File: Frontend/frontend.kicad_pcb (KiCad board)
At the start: 2 copper layers, 300 parts, among them J1 PCIEx4 EDGE, J2 SWD, J3 CONN-TE-1-1337543-0, J4 UMC, J5 UMC, J6 CONN-TE-1-1337543-0, J7 UMC, J8 UMC, K1 HE3600, K10 EE2-5NU, K11 EE2-5NU, K12 EE2-5NU, K2 EE2-5NU, K3 HE3600, K4 EE2-5NU, K5 EE2-5NU, K6 EE2-5NU, K7 HE3600, K8 EE2-5NU, K9 HE3600, Q1 ULN2003AD, Q2 ULN2003AD, U1 ADA4817-1ACPZ, U10 AD8602ARZ, U11 TL972PW, U12 AD8602ARZ, U13 STM32F030C8T, U14 TL972PW, U15 AD8602ARZ, U17 MCP1700T-5002E/MB, U2 AD8003ACPZ, U24 AP3211, U26 LT1931AES5, U27 MC79M05CDT, U28 TL431AIDBZ, U29 TL431AIDBZ, U3 LMH6552SD, U4 ADA4817-1ACPZ, U5 AD8003ACPZ, U6 LMH6552SD, U8 4051-DIP, U9 TL972PW

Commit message: Route PCB
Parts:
- removed the CV1 at (-17.0, 90.5)
- removed the CV1 at (19.8, 128.3)
- removed the CV3 at (140.5, 104.5)
- removed the CV3 at (19.8, 128.3)
- removed the CV5 at (156.0, 92.0)
- removed the CV5 at (19.8, 128.3)
- removed the CV7 at (30.8, 90.5)
- removed the CV7 at (19.8, 128.3)
- removed DZ2: 43V, IPC7351-Nominal:DIOM5226X203
- removed E8: 120, IPC7351-Nominal:RESC3216X60
- removed K10, K11, K12, K8: EE2-5NU, manuf:KEMET-EE2-xNU
- removed K7, K9: HE3600, manuf:HAMLIN-HE3600
- removed L1: 6u8, manuf:BOURNS-SRN5040
- removed L2, L3: 22u, manuf:BOURNS-SRN3015
- removed Q2: ULN2003AD, IPC7351-Nominal:SOIC127P600X150-16
- removed R128: 36k, IPC7351-Nominal:RESC1608X50
- removed R129: 5k6, IPC7351-Nominal:RESC1608X50
- removed R130, R134: 10k, IPC7351-Nominal:RESC1608X50
- removed R131: 2k, IPC7351-Nominal:RESC1608X50
- removed R132, R133: 200, IPC7351-Nominal:RESC1608X50
- removed R135, R137: 120, IPC7351-Nominal:RESC1608X50
- removed R136: 30, IPC7351-Nominal:RESC1608X50
- removed U17: MCP1700T-5002E/MB, smd-semi:SOT-89
- added C100: 10n, IPC7351-Nominal:CAPC1005X55, B.Cu at (132.5, 49.0)
- added C101: 10n, IPC7351-Nominal:CAPC1005X55, B.Cu at (129.8, 43.5)
- added C102: 10n, IPC7351-Nominal:CAPC1005X55, B.Cu at (125.0, 41.5)
- added C103: 10n, IPC7351-Nominal:CAPC1005X55, B.Cu at (121.8, 36.0)
- added C104: 100n, IPC7351-Nominal:CAPC1608X55, F.Cu at (106.5, 29.2)
- added C105: 100n, IPC7351-Nominal:CAPC1220X107, B.Cu at (124.5, 26.5)
- added C106: 10n, IPC7351-Nominal:CAPC1005X55, B.Cu at (121.0, 46.0)
- added C107: 10n, IPC7351-Nominal:CAPC1005X55, B.Cu at (126.2, 48.5)
- added C108: 10n, IPC7351-Nominal:CAPC1005X55, B.Cu at (130.1, 49.0)
- added C109: 10n, IPC7351-Nominal:CAPC1005X55, B.Cu at (132.0, 43.5)
- added C110: 10n, IPC7351-Nominal:CAPC1005X55, B.Cu at (122.5, 41.5)
- added C111: 10n, IPC7351-Nominal:CAPC1005X55, B.Cu at (124.2, 36.0)
- added C112: 100n, IPC7351-Nominal:CAPC1608X55, F.Cu at (116.8, 26.2)
- added C113: 100n, IPC7351-Nominal:CAPC1608X55, F.Cu at (126.8, 67.5)
- added C89: 100n, IPC7351-Nominal:CAPC1220X107, F.Cu at (131.5, 31.5)
- added C90: 100n, IPC7351-Nominal:CAPC1220X107, F.Cu at (133.8, 40.8)
- added C91: 100n, IPC7351-Nominal:CAPC1220X107, F.Cu at (134.5, 38.0)
- added C92: 33u/16, IPC7351-Nominal:CAPMP7343X310, F.Cu at (140.8, 39.2)
- added C93: 100n, IPC7351-Nominal:CAPC1220X107, F.Cu at (124.8, 55.5)
- added C94: 100n, IPC7351-Nominal:CAPC1220X107, F.Cu at (134.2, 33.8)
- added C95: 100n, IPC7351-Nominal:CAPC1220X107, F.Cu at (128.0, 40.5)
- added C96: 100n, IPC7351-Nominal:CAPC1220X107, F.Cu at (125.8, 33.2)
- added C97: 100n, IPC7351-Nominal:CAPC1220X107, B.Cu at (127.5, 26.5)
- added C98: 10n, IPC7351-Nominal:CAPC1005X55, B.Cu at (121.0, 48.5)
- added C99: 10n, IPC7351-Nominal:CAPC1005X55, B.Cu at (126.2, 45.2)
- added CV1: 30p, CV8, F.Cu at (114.5, 95.0)
- added CV3: 30p, CV8, F.Cu at (83.5, 72.0)
- added CV5: 30p, CV8, F.Cu at (114.5, 49.0)
- added CV7: 30p, CV8, F.Cu at (83.5, 26.0)
- added D6: BAV99W, smd-semi:SC-70, F.Cu at (113.0, 22.5)
- added D7: BAV99W, smd-semi:SC-70, F.Cu at (116.5, 23.5)
- added J10: SWD, conn-100mil:CONN-100MIL-M-2x5-SHROUD, F.Cu at (150.8, 57.5)
- added J11: APWR, conn-100mil:CONN-100MIL-M-1x4-SHROUD, B.Cu at (159.0, 25.8)
- added J9: PCIEx4 EDGE, w_conn_pc:pci-x_edge-x4, F.Cu at (110.0, 114.0)
- added U19: LM317S, smd-semi:TO-263, F.Cu at (151.0, 85.7)
- added U20: L78M05CDT, smd-semi:TO-252, F.Cu at (137.0, 26.0)
- added U21: MCP1700T-3302E/TT, smd-semi:SOT-23, F.Cu at (136.2, 72.0)
- added U22: MC79M05CDT, smd-semi:TO-252, F.Cu at (157.3, 39.6)
- added U23: MCP9700T-E/TT, smd-semi:SOT-23, F.Cu at (68.5, 55.5)
- added U25: MAX4567EEE, IPC7351-Nominal:SOP63P600X160-16, F.Cu at (123.8, 47.0)
- added U7: LMH6552SD, IPC7351-Nominal:PSON50P300X250X80-9, F.Cu at (126.0, 73.8)
- C1: value 6p8 -> 1u; footprint IPC7351-Nominal:CAPC1608X55 -> IPC7351-Nominal:CAPC2012X70
- C11: value 100n -> 33u/16; footprint IPC7351-Nominal:CAPC1608X55 -> IPC7351-Nominal:CAPMP7343X310
- C12, C13, C14, C15: footprint IPC7351-Nominal:CAPC1608X55 -> IPC7351-Nominal:CAPC1220X107
- C16: value 10p 1kV -> 33u/16; footprint IPC7351-Nominal:CAPC3216X70 -> IPC7351-Nominal:CAPMP7343X310
- C17: value 22n 630V -> 100n; footprint manuf:MANUF-PANASONIC-ECQ-EF -> IPC7351-Nominal:CAPC1220X107
- C18: value 6p8 -> 100n; footprint IPC7351-Nominal:CAPC1608X55 -> IPC7351-Nominal:CAPC1220X107; moved to F.Cu
- C19: value 4p7 1kV -> 100n; footprint IPC7351-Nominal:CAPC3216X70 -> IPC7351-Nominal:CAPC1220X107
- C2: value 22n 630V -> 6p8; footprint manuf:MANUF-PANASONIC-ECQ-EF -> IPC7351-Nominal:CAPC1608X55
- C20: value 10p 1kV -> 100n; footprint IPC7351-Nominal:CAPC3216X70 -> IPC7351-Nominal:CAPC1220X107
- C21: value 120p -> 100n; footprint IPC7351-Nominal:CAPC2012X70 -> IPC7351-Nominal:CAPC1220X107; moved to B.Cu
- C22, C23, C24, C25, C26, C27, C30, C31, C32, C33, C34: value 100n -> 10n; footprint IPC7351-Nominal:CAPC1608X55 -> IPC7351-Nominal:CAPC1005X55; moved to B.Cu
- C29: footprint IPC7351-Nominal:CAPC1608X55 -> IPC7351-Nominal:CAPC1220X107; moved to B.Cu
- C35: value 100n -> 10n; footprint pth-passive:C-FILM-2.5mm -> IPC7351-Nominal:CAPC1005X55; moved to B.Cu
- C37, C43: value 100n -> 15u/16; footprint pth-passive:C-FILM-2.5mm -> IPC7351-Nominal:CAPMP3528X210
- C38: value 100n -> 1u; footprint pth-passive:C-FILM-2.5mm -> IPC7351-Nominal:CAPC2012X70; moved to B.Cu
- C39: footprint pth-passive:C-FILM-2.5mm -> IPC7351-Nominal:CAPC1608X55
- C4: value 4p7 1kV -> 22n 630V; footprint IPC7351-Nominal:CAPC3216X70 -> manuf:MANUF-PANASONIC-ECQ-EF; moved to F.Cu
- C40, C42, C47, E5, J7, J8: moved to B.Cu
- C41: footprint pth-passive:C-FILM-2.5mm -> IPC7351-Nominal:CAPC1608X55; moved to B.Cu
- C44: value 10n -> 100n; footprint IPC7351-Nominal:CAPC2012X70 -> IPC7351-Nominal:CAPC1608X55
- C45: value 220u -> 15u/16; footprint pth-passive:C-ALUM-8mm -> IPC7351-Nominal:CAPMP3528X210
- C46: value 10u -> 1u; footprint IPC7351-Nominal:CAPC3216X70 -> IPC7351-Nominal:CAPC2012X70
- C48: value 47u -> 10n; footprint pth-passive:C-ALUM-5mm -> IPC7351-Nominal:CAPC1005X55
- C49: value 100n -> 10n; footprint IPC7351-Nominal:CAPC1608X55 -> IPC7351-Nominal:CAPC1005X55
- C5, R1: moved to F.Cu
- C50: value 22u -> 100n; footprint IPC7351-Nominal:CAPC3216X70 -> IPC7351-Nominal:CAPC1608X55
- C52, C54, C62, C64, C68: value 47u -> 100n; footprint pth-passive:C-ALUM-5mm -> IPC7351-Nominal:CAPC1608X55
- C55: value 1u -> 15u/16; footprint IPC7351-Nominal:CAPC3216X70 -> IPC7351-Nominal:CAPMP3528X210
- C56: value 220u -> 100n; footprint pth-passive:C-ALUM-8mm -> IPC7351-Nominal:CAPC1608X55
- C57: value 10u -> 100n; footprint IPC7351-Nominal:CAPC3216X70 -> IPC7351-Nominal:CAPC1608X55
- C6: value 120p -> 4p7 1kV; footprint IPC7351-Nominal:CAPC2012X70 -> IPC7351-Nominal:CAPC3216X70
- C60: value 22u -> 15u/16; footprint IPC7351-Nominal:CAPC3216X70 -> IPC7351-Nominal:CAPMP3528X210
- C66: value 470p -> 47u; footprint IPC7351-Nominal:CAPC1608X55 -> pth-passive:C-ALUM-5mm
- C69: value 4p7 1kV -> 47u; footprint IPC7351-Nominal:CAPC3216X70 -> pth-passive:C-ALUM-5mm
- C7: value 100n -> 10p 1kV; footprint IPC7351-Nominal:CAPC1608X55 -> IPC7351-Nominal:CAPC3216X70
- C70: value 10p 1kV -> 47u; footprint IPC7351-Nominal:CAPC3216X70 -> pth-passive:C-ALUM-5mm; moved to F.Cu
- C71, C72: value 22u -> 1u; footprint IPC7351-Nominal:CAPC3216X70 -> IPC7351-Nominal:CAPC2012X70
- C73, C75, C76: value 100n -> 47u; footprint IPC7351-Nominal:CAPC1608X55 -> pth-passive:C-ALUM-5mm
- C78: value 1u -> 6p8; footprint IPC7351-Nominal:CAPC2012X70 -> IPC7351-Nominal:CAPC1608X55
- C79: value 1u -> 4p7 1kV; footprint IPC7351-Nominal:CAPC2012X70 -> IPC7351-Nominal:CAPC3216X70
- C8: value 100n -> 120p; footprint IPC7351-Nominal:CAPC1608X55 -> IPC7351-Nominal:CAPC2012X70; moved to B.Cu
- C80: value 1u -> 22n 630V; footprint IPC7351-Nominal:CAPC2012X70 -> manuf:MANUF-PANASONIC-ECQ-EF
- C81, C83: value 1u -> 10p 1kV; footprint IPC7351-Nominal:CAPC2012X70 -> IPC7351-Nominal:CAPC3216X70
- C82: value 1u -> 4p7 1kV; footprint IPC7351-Nominal:CAPC2012X70 -> IPC7351-Nominal:CAPC3216X70; moved to B.Cu
- C84: value 1u -> 120p; moved to B.Cu
- C85, C86: value 1u -> 100n; footprint IPC7351-Nominal:CAPC2012X70 -> IPC7351-Nominal:CAPC1608X55
- C87: value 1u -> 33u/16; footprint IPC7351-Nominal:CAPC2012X70 -> IPC7351-Nominal:CAPMP7343X310
- C88: value 1u -> 100n; footprint IPC7351-Nominal:CAPC2012X70 -> IPC7351-Nominal:CAPC1220X107
- CV2, CV4, CV6, CV8: footprint CV1 -> CV8
- D1, D2: value BAV99 -> BAV99W; footprint smd-semi:SOT-23 -> smd-semi:SC-70
- D3: value S1A -> BAV99W; footprint IPC7351-Nominal:DIOM5326X292 -> smd-semi:SC-70
- D4: value MBR0520 -> US1A; footprint smd-semi:SOD-123 -> IPC7351-Nominal:DIOM5326X292
- D5: value MBR0520 -> BAV99W; footprint smd-semi:SOD-123 -> smd-semi:SC-70
- E2, E3: value 120 -> BEAD-0603; footprint IPC7351-Nominal:RESC3216X60 -> IPC7351-Nominal:INDC1608X95
- J1: value PCIEx4 EDGE -> VOCM; footprint conn-fci:CONN-10018784-10201TLF-PCIEx4-FCI -> conn-100mil:CONN-100MIL-M-1x2; moved to B.Cu
- J2: value SWD -> BNC; footprint conn-100mil:CONN-100MIL-M-2x5-SHROUD -> manuf:CONN-BNC-1-1337543-0
- J3: value CONN-TE-1-1337543-0 -> UMC; footprint manuf:CONN-BNC-1-1337543-0 -> conn-molex:CONN-MOLEX-0734120110; moved to B.Cu
- J5: value UMC -> VOCM; footprint conn-molex:CONN-MOLEX-0734120110 -> conn-100mil:CONN-100MIL-M-1x2
- J6: value CONN-TE-1-1337543-0 -> BNC
- K4, K6: value EE2-5NU -> HE3600; footprint manuf:KEMET-EE2-xNU -> manuf:HAMLIN-HE3600
- MP1: value SHIELD -> 217-36CTE6; footprint manuf:LAIRD-BMI-S-203 -> MP1
- R10: value 523k -> 536k
- R100: value 430 -> 200; footprint IPC7351-Nominal:RESC1608X50 -> IPC7351-Nominal:RESC3216X60
- R101: value 1k -> 200; footprint IPC7351-Nominal:RESC1608X50 -> IPC7351-Nominal:RESC3216X60
- R102, R103: value 10k -> 200; footprint IPC7351-Nominal:RESC1608X50 -> IPC7351-Nominal:RESC3216X60
- R104: value 20k -> 10M; moved to B.Cu
- R105: value 430 -> 3k3; footprint IPC7351-Nominal:RESC1608X50 -> IPC7351-Nominal:RESC1005X40
- R106, R107: value 1k -> 357k; footprint IPC7351-Nominal:RESC1608X50 -> IPC7351-Nominal:RESC2012X50; moved to B.Cu
- R108: value 10k -> 150; footprint IPC7351-Nominal:RESC1608X50 -> IPC7351-Nominal:RESC1005X40
- R109: value 20k -> 348k; footprint IPC7351-Nominal:RESC1608X50 -> IPC7351-Nominal:RESC2012X50; moved to B.Cu
- R11: value 536k -> 100k; footprint IPC7351-Nominal:RESC2012X50 -> IPC7351-Nominal:RESC1608X50; moved to F.Cu
- R110: value 30k -> 10M; moved to B.Cu
- R111: value 1k -> 348k; footprint IPC7351-Nominal:RESC1608X50 -> IPC7351-Nominal:RESC2012X50; moved to B.Cu
- R112: value 3k3 -> 150; footprint IPC7351-Nominal:RESC1608X50 -> IPC7351-Nominal:RESC1005X40
- R113: value 3k3 -> 443; footprint IPC7351-Nominal:RESC1608X50 -> IPC7351-Nominal:RESC1005X40
- R114, R124: value 10k -> 49R9; footprint IPC7351-Nominal:RESC1608X50 -> IPC7351-Nominal:RESC1005X40
- R115: value 10k -> 165; footprint IPC7351-Nominal:RESC1608X50 -> IPC7351-Nominal:RESC1005X40
- R116: value 20k -> 443; footprint IPC7351-Nominal:RESC1608X50 -> IPC7351-Nominal:RESC1005X40
- R117: value 30k -> 64R9; footprint IPC7351-Nominal:RESC1608X50 -> IPC7351-Nominal:RESC1005X40
- R118: value 10k -> 300; footprint IPC7351-Nominal:RESC1608X50 -> IPC7351-Nominal:RESC1005X40
- R119: value 10k -> 35R7; footprint IPC7351-Nominal:RESC1608X50 -> IPC7351-Nominal:RESC1005X40
- R12: value 357k -> 10M; footprint IPC7351-Nominal:RESC2012X50 -> IPC7351-Nominal:RESC1608X50; moved to F.Cu
- R120: value 10k -> 64R9; footprint IPC7351-Nominal:RESC1608X50 -> IPC7351-Nominal:RESC1005X40
- R121: value 20k -> 300; footprint IPC7351-Nominal:RESC1608X50 -> IPC7351-Nominal:RESC1005X40
- R122: value 100 -> 150; footprint IPC7351-Nominal:RESC1608X50 -> IPC7351-Nominal:RESC1005X40
- R123: value 10k -> 443; footprint IPC7351-Nominal:RESC1608X50 -> IPC7351-Nominal:RESC1005X40
- R125: value 20k -> 120k; footprint IPC7351-Nominal:RESC1608X50 -> IPC7351-Nominal:RESC1005X40
- R126: value 100 -> 443; footprint IPC7351-Nominal:RESC1608X50 -> IPC7351-Nominal:RESC1005X40
- R127: value 120 -> 30k; footprint IPC7351-Nominal:RESC1608X50 -> IPC7351-Nominal:RESC1005X40
- R14: value 200 -> 357k; footprint IPC7351-Nominal:RESC3216X60 -> IPC7351-Nominal:RESC2012X50; moved to B.Cu
- R18: value 100k -> 200; footprint IPC7351-Nominal:RESC1608X50 -> IPC7351-Nominal:RESC3216X60
- R19: value 357k -> 10M; footprint IPC7351-Nominal:RESC2012X50 -> IPC7351-Nominal:RESC1608X50
- R20: value 357k -> 3k3; footprint IPC7351-Nominal:RESC2012X50 -> IPC7351-Nominal:RESC1005X40; moved to F.Cu
- R21: value 348k -> 357k
- R22: value 10M -> 357k
- R23: value 348k -> 150; footprint IPC7351-Nominal:RESC2012X50 -> IPC7351-Nominal:RESC1005X40; moved to F.Cu
- R24: value 10M -> 348k; moved to B.Cu
- R25: value 120 -> 10M; moved to B.Cu
- R26: value 120 -> 348k; footprint IPC7351-Nominal:RESC1608X50 -> IPC7351-Nominal:RESC2012X50; moved to B.Cu
- R27: value 443 -> 150; footprint IPC7351-Nominal:RESC1608X50 -> IPC7351-Nominal:RESC1005X40
- R28: value 49r9 -> 443; footprint IPC7351-Nominal:RESC1608X50 -> IPC7351-Nominal:RESC1005X40
- R29: value 30 -> 49R9; footprint IPC7351-Nominal:RESC1608X50 -> IPC7351-Nominal:RESC1005X40
- R30, R33, R35, R38, R4: footprint IPC7351-Nominal:RESC1608X50 -> IPC7351-Nominal:RESC1005X40
- R31: value 30 -> 443; footprint IPC7351-Nominal:RESC1608X50 -> IPC7351-Nominal:RESC1005X40
- R32: value 30 -> 64R9; footprint IPC7351-Nominal:RESC1608X50 -> IPC7351-Nominal:RESC1005X40
- R34: value 300 -> 35R7; footprint IPC7351-Nominal:RESC1608X50 -> IPC7351-Nominal:RESC1005X40
- R36: value 64R9 -> 300; footprint IPC7351-Nominal:RESC1608X50 -> IPC7351-Nominal:RESC1005X40
- R37: value 120 -> 150; footprint IPC7351-Nominal:RESC1608X50 -> IPC7351-Nominal:RESC1005X40
- R39: value 49r9 -> 49R9; footprint IPC7351-Nominal:RESC1608X50 -> IPC7351-Nominal:RESC1005X40
- R40: value 200 -> 120k; footprint IPC7351-Nominal:RESC1608X50 -> IPC7351-Nominal:RESC1005X40
- R41: value 35R7 -> 443; footprint IPC7351-Nominal:RESC1608X50 -> IPC7351-Nominal:RESC1005X40
- R42: value 432 -> 30k; footprint IPC7351-Nominal:RESC1608X50 -> IPC7351-Nominal:RESC1005X40
- R43, R44: value 75 -> 10k
- R45: value 1M -> 10k
- R46: value 120 -> 47k
- R47, R48: value 332k -> 47k; footprint IPC7351-Nominal:RESC2012X50 -> IPC7351-Nominal:RESC1608X50
- R49: value 332k -> 10k; footprint IPC7351-Nominal:RESC2012X50 -> IPC7351-Nominal:RESC1005X40
- R50: value 3k3 -> 33k; footprint IPC7351-Nominal:RESC1608X50 -> IPC7351-Nominal:RESC1005X40
- R51: value 523k -> 10k; footprint IPC7351-Nominal:RESC2012X50 -> IPC7351-Nominal:RESC1005X40
- R52: value 523k -> 33k; footprint IPC7351-Nominal:RESC2012X50 -> IPC7351-Nominal:RESC1005X40
- R53: value 536k -> 20k; footprint IPC7351-Nominal:RESC2012X50 -> IPC7351-Nominal:RESC1005X40
- R54: value 357k -> 5k6; footprint IPC7351-Nominal:RESC2012X50 -> IPC7351-Nominal:RESC1005X40
- R55: value 357k -> 20k; footprint IPC7351-Nominal:RESC2012X50 -> IPC7351-Nominal:RESC1005X40
- R56, R57, R58, R59: value 200 -> 5k6; footprint IPC7351-Nominal:RESC3216X60 -> IPC7351-Nominal:RESC1005X40
- R60: value 100k -> 5k6; footprint IPC7351-Nominal:RESC1608X50 -> IPC7351-Nominal:RESC1005X40
- R61: value 357k -> 10k; footprint IPC7351-Nominal:RESC2012X50 -> IPC7351-Nominal:RESC1005X40
- R62: value 357k -> 680; footprint IPC7351-Nominal:RESC2012X50 -> IPC7351-Nominal:RESC1005X40
- R63: value 348k -> 10k; footprint IPC7351-Nominal:RESC2012X50 -> IPC7351-Nominal:RESC1005X40
- R64: value 10M -> 680; footprint IPC7351-Nominal:RESC2012X50 -> IPC7351-Nominal:RESC1005X40
- R65: value 348k -> 20k; footprint IPC7351-Nominal:RESC2012X50 -> IPC7351-Nominal:RESC1005X40
- R66, R82: value 30 -> 5k6; footprint IPC7351-Nominal:RESC1608X50 -> IPC7351-Nominal:RESC1005X40
- R67: value 33 -> 20k; footprint IPC7351-Nominal:RESC1608X50 -> IPC7351-Nominal:RESC1005X40
- R68, R72: value 120 -> 5k6; footprint IPC7351-Nominal:RESC1608X50 -> IPC7351-Nominal:RESC1005X40
- R69, R80: value 443 -> 5k6; footprint IPC7351-Nominal:RESC1608X50 -> IPC7351-Nominal:RESC1005X40
- R70, R81: value 49r9 -> 5k6; footprint IPC7351-Nominal:RESC1608X50 -> IPC7351-Nominal:RESC1005X40
- R71: value 10M -> 5k6; footprint IPC7351-Nominal:RESC2012X50 -> IPC7351-Nominal:RESC1005X40; moved to F.Cu
- R73: value 30 -> 10k; footprint IPC7351-Nominal:RESC1608X50 -> IPC7351-Nominal:RESC1005X40; moved to F.Cu
- R74: value 165 -> 100; footprint IPC7351-Nominal:RESC1608X50 -> IPC7351-Nominal:RESC1005X40; moved to F.Cu
- R75: value 300 -> 10k; footprint IPC7351-Nominal:RESC1608X50 -> IPC7351-Nominal:RESC1005X40
- R76: value 300 -> 100; footprint IPC7351-Nominal:RESC1608X50 -> IPC7351-Nominal:RESC1005X40
- R77: value 64R9 -> 20k; footprint IPC7351-Nominal:RESC1608X50 -> IPC7351-Nominal:RESC1005X40
- R78: value 64R9 -> 5k6; footprint IPC7351-Nominal:RESC1608X50 -> IPC7351-Nominal:RESC1005X40
- R79: value 120 -> 20k; footprint IPC7351-Nominal:RESC1608X50 -> IPC7351-Nominal:RESC1005X40
- R8: value 3k3 -> 523k; footprint IPC7351-Nominal:RESC1608X50 -> IPC7351-Nominal:RESC2012X50; moved to B.Cu
- R83: value 30 -> 15 2W; footprint IPC7351-Nominal:RESC1608X50 -> manuf:KOASPEER-MOS-2W
- R84: value 432 -> 120
- R85: value 200 -> 430; moved to F.Cu
- R86: value 15k -> 75
- R87: value 10k -> 75
- R88: value 35R7 -> 1M; moved to F.Cu
- R89: value 15k -> 33; footprint IPC7351-Nominal:RESC1608X50 -> IPC7351-Nominal:RESC1005X40
- R90, R91: value 10k -> 332k; footprint IPC7351-Nominal:RESC1608X50 -> IPC7351-Nominal:RESC2012X50
- R92: value 120 -> 332k; footprint IPC7351-Nominal:RESC1608X50 -> IPC7351-Nominal:RESC2012X50
- R93, R94: value 47k -> 523k; footprint IPC7351-Nominal:RESC1608X50 -> IPC7351-Nominal:RESC2012X50; moved to B.Cu
- R95: value 47k -> 536k; footprint IPC7351-Nominal:RESC1608X50 -> IPC7351-Nominal:RESC2012X50; moved to B.Cu
- R96: value 10k -> 100k
- R97: value 10k -> 10M
- R98: value 10k -> 357k; footprint IPC7351-Nominal:RESC1608X50 -> IPC7351-Nominal:RESC2012X50; moved to B.Cu
- R99: value 20k -> 357k; footprint IPC7351-Nominal:RESC1608X50 -> IPC7351-Nominal:RESC2012X50; moved to B.Cu
- U1: value ADA4817-1ACPZ -> MCP9700T-E/TT; footprint manuf:ANALOG-LFCSP_VD-8 -> smd-semi:SOT-23
- U10: value AD8602ARZ -> STM32F030C8T; footprint IPC7351-Nominal:SOIC127P600X175-8 -> IPC7351-Nominal:QFP50P900X900X160-48
- U11, U14: value TL972PW -> MC33078DGK; footprint IPC7351-Nominal:SOP65P640X120-8 -> IPC7351-Nominal:SOP65P490X109-8
- U12, U15: value AD8602ARZ -> MC33078DGK; footprint IPC7351-Nominal:SOIC127P600X175-8 -> IPC7351-Nominal:SOP65P490X109-8
- U13: value STM32F030C8T -> MC33078DGK; footprint IPC7351-Nominal:QFP50P900X900X160-48 -> IPC7351-Nominal:SOP65P490X109-8
- U2: value AD8003ACPZ -> ADA4817-1ACPZ; footprint IPC7351-Nominal:QFN50P400X400X80-25 -> manuf:ANALOG-LFCSP_VD-8
- U24: value AP3211 -> ADA4817-1ACPZ; footprint smd-semi:SOT-23-6 -> manuf:ANALOG-LFCSP_VD-8
- U26: value LT1931AES5 -> MAX4567EEE; footprint smd-semi:SOT-23-5 -> IPC7351-Nominal:SOP63P600X160-16
- U27: value MC79M05CDT -> AD8003ACPZ; footprint smd-semi:TO-252 -> IPC7351-Nominal:QFN50P400X400X80-25
- U28: value TL431AIDBZ -> MAX4567EEE; footprint smd-semi:SOT-23 -> IPC7351-Nominal:SOP63P600X160-16
- U29: value TL431AIDBZ -> LMH6552SD; footprint smd-semi:SOT-23 -> IPC7351-Nominal:PSON50P300X250X80-9
- U3, U6: value LMH6552SD -> MAX4567EEE; footprint IPC7351-Nominal:PSON50P300X250X80-9 -> IPC7351-Nominal:SOP63P600X160-16
- U4: value ADA4817-1ACPZ -> MAX4567EEE; footprint manuf:ANALOG-LFCSP_VD-8 -> IPC7351-Nominal:SOP63P600X160-16
- U8: value 4051-DIP -> MC33078DGK; footprint dip-sip:DIP-16 -> IPC7351-Nominal:SOP65P490X109-8
- U9: value TL972PW -> MAX5725AAUP; footprint IPC7351-Nominal:SOP65P640X120-8 -> IPC7351-Nominal:SOP65P640X110-20
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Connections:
- C1 pad 1: Net-(C1-Pad1) -> +5
- C1 pad 2: Net-(C1-Pad2) -> GND
- C10 pad 1: +5 -> Net-(C10-Pad1)
- C12 pad 1: -5 -> +5
- C13 pad 1: -5 -> +5
- C14 pad 1: -5 -> +5
- C15 pad 1: -5 -> +5
- C16 pad 1: Net-(C16-Pad1) -> GND
- C16 pad 2: Net-(C16-Pad2) -> -5
- C17 pad 1: Net-(C17-Pad1) -> GND
- C17 pad 2: Net-(C17-Pad2) -> -5
- C18 pad 1: Net-(C18-Pad1) -> GND
- C18 pad 2: Net-(C18-Pad2) -> -5
- C19 pad 1: Net-(C19-Pad1) -> GND
- C19 pad 2: Net-(C19-Pad2) -> -5
- C20 pad 1: Net-(C19-Pad2) -> GND
- C20 pad 2: Net-(C20-Pad2) -> -5
- C21 pad 1: Net-(C19-Pad1) -> +5
- C22 pad 1: Net-(C22-Pad1) -> +5
- C27 pad 1: -5 -> +5
- C28 pad 1: -5 -> +8
- C29 pad 1: -5 -> GND
- C29 pad 2: GND -> -5
- C3 pad 2: Net-(C16-Pad1) -> Net-(C3-Pad2)
- C30 pad 1: -5 -> GND
- C30 pad 2: GND -> -5
- C31 pad 1: Net-(C31-Pad1) -> GND
- C31 pad 2: GND -> -5
- C32 pad 1: Net-(C32-Pad1) -> GND
- C32 pad 2: GND -> -5
- C33 pad 1: +2.5 -> GND
- C33 pad 2: GND -> -5
- C34 pad 1: Net-(C34-Pad1) -> GND
- C34 pad 2: GND -> -5
- C35 pad 1: Net-(C35-Pad1) -> GND
- C35 pad 2: GND -> -5
- C36 pad 1: Net-(C36-Pad1) -> GND
- C36 pad 2: GND -> -8
- C37 pad 1: Net-(C37-Pad1) -> +3.3
- C38 pad 1: Net-(C38-Pad1) -> +3.3
- C39 pad 1: Net-(C39-Pad1) -> +3.3
- C40 pad 1: Net-(C40-Pad1) -> +3.3
- C41 pad 1: Net-(C41-Pad1) -> +3.3
- C42 pad 1: Net-(C42-Pad1) -> +3.3
- C43 pad 1: Net-(C43-Pad1) -> /Microcontroller/3V3DAC
- C44 pad 1: Net-(C44-Pad1) -> GND
- C44 pad 2: Net-(C44-Pad2) -> /Microcontroller/3V3DAC
- C45 pad 1: Net-(C45-Pad1) -> /Microcontroller/3V3ADC
- C46 pad 1: Net-(C45-Pad1) -> /Microcontroller/3V3ADC
- C47 pad 1: Net-(C45-Pad1) -> GND
- C47 pad 2: GND -> /Microcontroller/3V3ADC
- C48 pad 1: Net-(C48-Pad1) -> /Channel1/VOS1
- C48 pad 2: GND -> Net-(C48-Pad2)
- C49 pad 1: Net-(C49-Pad1) -> /Channel2/VOS1
- C49 pad 2: GND -> Net-(C49-Pad2)
- C5 pad 1: Net-(C4-Pad2) -> Net-(C3-Pad2)
- C50 pad 1: Net-(C49-Pad1) -> -2.5
- C50 pad 2: GND -> Net-(C50-Pad2)
- C51 pad 1: Net-(C51-Pad1) -> /Channel1/VOS2
- C51 pad 2: GND -> Net-(C51-Pad2)
- C52 pad 1: Net-(C51-Pad1) -> /Channel2/VOS2
- C52 pad 2: GND -> Net-(C52-Pad2)
- C53 pad 1: Net-(C53-Pad1) -> /Channel1/VOS3
- C53 pad 2: GND -> Net-(C53-Pad2)
- C54 pad 1: Net-(C53-Pad1) -> /Channel2/VOS3
- C54 pad 2: GND -> Net-(C54-Pad2)
- C55 pad 1: Net-(C55-Pad1) -> +8
- C55 pad 2: Net-(C55-Pad2) -> GND
- C56 pad 1: Net-(C56-Pad1) -> +8
- C57 pad 1: Net-(C56-Pad1) -> +8
- C58 pad 1: Net-(C56-Pad1) -> +8
- C59 pad 1: Net-(C59-Pad1) -> +8
- C6 pad 1: Net-(C4-Pad1) -> Net-(C6-Pad1)
- C6 pad 2: GND -> Net-(C6-Pad2)
- C60 pad 1: Net-(C59-Pad1) -> GND
- C60 pad 2: GND -> -8
- C61 pad 1: Net-(C61-Pad1) -> GND
- C61 pad 2: GND -> -8
- C62 pad 2: Net-(C61-Pad1) -> -8
- C63 pad 1: Net-(C63-Pad1) -> GND
- C63 pad 2: GND -> -8
- C64 pad 2: Net-(C63-Pad1) -> -8
- C65 pad 1: GND -> Net-(C65-Pad1)
- C65 pad 2: -5 -> GND
- C66 pad 1: Net-(C59-Pad1) -> /Power/VRHS
- C66 pad 2: Net-(C66-Pad2) -> GND
- C67 pad 1: +2.5 -> +8
- C68 pad 1: GND -> Net-(C68-Pad1)
- C68 pad 2: -2.5 -> GND
- C69 pad 1: Net-(C69-Pad1) -> Net-(C68-Pad1)
- C69 pad 2: Net-(C69-Pad2) -> GND
- C7 pad 1: Net-(C7-Pad1) -> Net-(C6-Pad2)
- C7 pad 2: GND -> Net-(C7-Pad2)
- C70 pad 1: Net-(C69-Pad2) -> +5
- C70 pad 2: Net-(C70-Pad2) -> GND
- C72 pad 1: +3.3 -> +3.3A
- C73 pad 1: +3.3 -> GND
- C73 pad 2: GND -> -8
- C74 pad 1: +3.3 -> Net-(C74-Pad1)
- C75 pad 1: +3.3 -> GND
- C75 pad 2: GND -> Net-(C74-Pad1)
- C76 pad 1: +3.3 -> GND
- C76 pad 2: GND -> -5
- C78 pad 1: +5 -> Net-(C78-Pad1)
- C78 pad 2: GND -> Net-(C78-Pad2)
- C79 pad 1: +5 -> Net-(C79-Pad1)
- C79 pad 2: GND -> Net-(C79-Pad2)
- C8 pad 1: +5 -> Net-(C6-Pad1)
- C80 pad 1: +5 -> Net-(C80-Pad1)
- C80 pad 2: GND -> Net-(C80-Pad2)
- C81 pad 1: +5 -> Net-(C79-Pad2)
- C81 pad 2: GND -> Net-(C81-Pad2)
- C82 pad 1: +5 -> Net-(C82-Pad1)
- C82 pad 2: GND -> Net-(C82-Pad2)
- C83 pad 1: GND -> Net-(C82-Pad2)
- C83 pad 2: -5 -> Net-(C83-Pad2)
- C84 pad 1: GND -> Net-(C82-Pad1)
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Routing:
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- added copper zone on F.Cu, net +5
- added copper zone on F.Cu, net -5
- added copper zone on F.Cu, net /Power/VRHS
- added copper zone on F.Cu, net GND
- added copper zone on In1.Cu, net GND
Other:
- board outline added: 100 x 100.2 mm
- copper layers 2 -> 4
- net class Default: clearance 0.2 -> 0.18
- rule trace_clearance: 0.2 -> 0.18

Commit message: Work more on routing
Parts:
- added DS1: LED-0603, smd-semi:LED-0603, F.Cu at (64.5, 61.0)
- added DS10: LED-0603, smd-semi:LED-0603, F.Cu at (128.5, 104.0)
- added DS11: LED-0603, smd-semi:LED-0603, F.Cu at (128.5, 107.0)
- added DS12: LED-0603, smd-semi:LED-0603, F.Cu at (128.5, 105.5)
- added DS2: LED-0603, smd-semi:LED-0603, F.Cu at (64.5, 62.5)
- added DS3: LED-0603, smd-semi:LED-0603, F.Cu at (64.5, 64.0)
- added DS4: LED-0603, smd-semi:LED-0603, F.Cu at (64.5, 65.5)
- added DS5: LED-0603, smd-semi:LED-0603, F.Cu at (64.5, 67.0)
- added DS6: LED-0603, smd-semi:LED-0603, F.Cu at (64.5, 68.5)
- added DS7: LED-0603, smd-semi:LED-0603, F.Cu at (143.2, 48.0)
- added DS8: LED-0603, smd-semi:LED-0603, F.Cu at (143.2, 46.5)
- added DS9: LED-0603, smd-semi:LED-0603, F.Cu at (143.2, 49.5)
- added G***: LOGO, LOGO, F.Cu at (68.0, 25.0)
- added R128: 3k3, IPC7351-Nominal:RESC1005X40, F.Cu at (68.0, 61.0)
- added R129: 3k3, IPC7351-Nominal:RESC1005X40, F.Cu at (68.0, 62.5)
- added R130: 3k3, IPC7351-Nominal:RESC1005X40, F.Cu at (68.0, 64.0)
- added R131: 3k3, IPC7351-Nominal:RESC1005X40, F.Cu at (68.0, 65.5)
- added R132: 3k3, IPC7351-Nominal:RESC1005X40, F.Cu at (68.0, 67.0)
- added R133: 3k3, IPC7351-Nominal:RESC1005X40, F.Cu at (68.0, 68.5)
- added R134: 3k3, IPC7351-Nominal:RESC1005X40, F.Cu at (140.1, 48.0)
- added R135: 3k3, IPC7351-Nominal:RESC1005X40, F.Cu at (140.0, 46.5)
- added R136: 3k3, IPC7351-Nominal:RESC1005X40, F.Cu at (140.0, 49.5)
- added R137: 3k3, IPC7351-Nominal:RESC1005X40, F.Cu at (125.3, 104.0)
- added R138: 3k3, IPC7351-Nominal:RESC1005X40, F.Cu at (125.3, 107.0)
- added R139: 3k3, IPC7351-Nominal:RESC1005X40, F.Cu at (125.2, 105.5)
- added TP1: INFO, conn-test:TEST-SMD-SMALL, F.Cu at (140.0, 52.0)
- added TP2: V1C1, conn-test:TEST-SMD-SMALL, F.Cu at (90.5, 55.5)
- added TP3: V1C2, conn-test:TEST-SMD-SMALL, F.Cu at (89.5, 68.0)
- added TP4: V2C1, conn-test:TEST-SMD-SMALL, F.Cu at (108.8, 54.0)
- added TP5: V2C2, conn-test:TEST-SMD-SMALL, F.Cu at (94.0, 68.0)
- added TP6: V3C1, conn-test:TEST-SMD-SMALL, F.Cu at (106.5, 54.0)
- added TP7: V3C2, conn-test:TEST-SMD-SMALL, F.Cu at (103.2, 68.0)
- moved DZ1 2.92 mm to (73.5, 73.5)
- moved Q1 2.92 mm to (73.5, 65.5)
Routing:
- net GND: track 404.7 -> 1390.2 mm, vias 235 -> 477
- net /Microcontroller/CH2_GAIN2: track 46.3 -> 75.7 mm, vias 2 -> 4
- net /Channel2/GUARD: track 61.8 -> 88.8 mm, vias 0 -> 2
- net /Channel1/GUARD: track 63.2 -> 88.2 mm, vias 0 -> 2
- net /Microcontroller/TX: track 0.00 -> 24.2 mm, vias 0 -> 2
- net /Microcontroller/CH2_GAIN1: track 81.3 -> 101.6 mm, vias 2 -> 4
- net -5: track 268.2 -> 286.4 mm
- net /Channel2/ATT2: track 44.0 -> 61.9 mm, vias 2 -> 4
- net /Channel1/ATT2: track 27.0 -> 40.7 mm, vias 2 -> 3
- net /Microcontroller/CH1_GAIN2: track 37.6 -> 49.4 mm, vias 4 -> 5
- net +5: track 472.0 -> 483.8 mm
- net (no net): track 0.00 -> 8.10 mm
- net /Microcontroller/CH1_TEMP: track 91.6 -> 83.8 mm
- net /Channel1/#DC: track 57.8 -> 50.7 mm
- net /Microcontroller/CH1_GAIN1: track 20.3 -> 25.7 mm
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- added copper zone on F.Cu, net +3.3
- added copper zone on In2.Cu, net +3.3
- added copper zone on In2.Cu, net +8
- added copper zone on In2.Cu, net -8
- added copper zone on B.Cu, net GND
- added copper zone on In2.Cu, net GND
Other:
- rule trace_min: 0.2 -> 0.16
- board text added: "1"
- board text added: "2"
- board text added: "3"
- board text added: "4"
- board text added: "ATT1"
- board text added: "ATT2"
- board text added: "CH1"
- board text added: "CH2"
- board text added: "DC"
- board text added: "GAIN1"
- board text added: "GAIN2"
- board text added: "INFO"
- board text added: "N"
- board text added: "OS-1 FRONTEND"
- board text added: "P"
- board text added: "REV A"
- board text added: "TERM"
- board text added: "THIS SPACE INTENTIONALLY LEFT BLANK"
- board text added: "V1C1"
- board text added: "V1C2"
- board text added: "V2C1"
- board text added: "V2C2"
- board text added: "V3C1"
- board text added: "V3C2"

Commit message: More layout work
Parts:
- removed C46: 1u, IPC7351-Nominal:CAPC2012X70
- removed C69, C75: 47u, pth-passive:C-ALUM-5mm
- removed C92: 33u/16, IPC7351-Nominal:CAPMP7343X310
- removed E5, E7: 120, IPC7351-Nominal:RESC3216X60
- removed U21: MCP1700T-3302E/TT, smd-semi:SOT-23
- added C114: TBD, IPC7351-Nominal:CAPC1005X55, F.Cu at (132.4, 87.0)
- added C115: TBD, IPC7351-Nominal:CAPC1005X55, F.Cu at (132.7, 41.0)
- added C116: TBD, IPC7351-Nominal:CAPC1005X55, F.Cu at (137.5, 80.2)
- added C117: TBD, IPC7351-Nominal:CAPC1005X55, F.Cu at (137.5, 34.2)
- added C118: 1u, IPC7351-Nominal:CAPC2012X70, F.Cu at (144.9, 70.5)
- added C119: 1u, IPC7351-Nominal:CAPC2012X70, F.Cu at (148.0, 29.5)
- added R140: TBD, IPC7351-Nominal:RESC1005X40, F.Cu at (130.8, 87.6)
- added R141: TBD, IPC7351-Nominal:RESC1005X40, F.Cu at (131.0, 41.6)
- added R142: TBD, IPC7351-Nominal:RESC1005X40, F.Cu at (136.4, 80.2)
- added R143: TBD, IPC7351-Nominal:RESC1005X40, F.Cu at (136.4, 34.2)
- added R144: 3k3, IPC7351-Nominal:RESC1005X40, F.Cu at (140.0, 43.5)
- added R145: 1k, IPC7351-Nominal:RESC1005X40, F.Cu at (140.0, 45.0)
- added R146: 3k3, IPC7351-Nominal:RESC1005X40, F.Cu at (137.2, 43.5)
- added R147: 3k3, IPC7351-Nominal:RESC1005X40, F.Cu at (137.2, 45.0)
- added R148: 100k, IPC7351-Nominal:RESC1608X50, F.Cu at (137.2, 73.0)
- added U16: MCP9700T-E/TT, smd-semi:SOT-23, F.Cu at (145.0, 73.8)
- added U17: MCP9700T-E/TT, smd-semi:SOT-23, F.Cu at (152.5, 29.5)
- added U18: TLV70233DSE, manuf:TEXAS-S-PWSON-N6, F.Cu at (137.0, 71.0)
- C43, C45: value 15u/16 -> 2u2; footprint IPC7351-Nominal:CAPMP3528X210 -> IPC7351-Nominal:CAPMP2013X120
- C47: moved to F.Cu
- C67, C73: value 47u -> 330u; footprint pth-passive:C-ALUM-5mm -> pth-passive:C-ALUM-8mm
- moved C67 22.0 mm to (157.0, 43.5)
- moved U22 18.8 mm to (147.5, 23.5), turned to 0 degrees
- moved C74 17.4 mm to (144.0, 28.5), turned to 180 degrees
- moved U20 14.1 mm to (147.5, 35.5), turned to 0 degrees
- moved C73 13.0 mm to (137.5, 23.0)
- moved E4 12.4 mm to (157.5, 34.0), turned to 270 degrees
- moved C76 11.7 mm to (139.0, 30.5)
- moved C70 10.8 mm to (146.5, 42.5)
- moved E6 9.66 mm to (158.0, 20.0)
- moved C37 8.96 mm to (142.5, 64.5), turned to 0 degrees
- moved E3 6.83 mm to (144.2, 59.5), turned to 180 degrees
- moved C72 5.20 mm to (137.0, 69.0), turned to 0 degrees
- moved C68 5.06 mm to (144.0, 30.5)
- moved C45 3.16 mm to (141.2, 60.0), turned to 270 degrees
- moved C43 2.93 mm to (120.8, 68.0)
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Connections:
- C68 pad 1: Net-(C68-Pad1) -> +8
- C74 pad 1: Net-(C74-Pad1) -> -8
- U10 pad 12: Net-(U10-Pad12) -> /Microcontroller/+5VMON
- U10 pad 13: Net-(U10-Pad13) -> /Microcontroller/-5VMON
- U10 pad 14: Net-(U10-Pad14) -> /Microcontroller/TEMP_VRELAY
- U10 pad 15: Net-(U10-Pad15) -> /Microcontroller/TEMP_V5
- U20 pad 1: Net-(C68-Pad1) -> +8
- U22 pad 3: Net-(C74-Pad1) -> -8
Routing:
- net GND: track 1390.2 -> 1256.5 mm, vias 477 -> 422
- net +3.3: track 164.6 -> 102.4 mm, vias 12 -> 15
- net /Microcontroller/TEMP_V5: track 0.00 -> 38.4 mm, vias 0 -> 2
- net /Microcontroller/TEMP_VRELAY: track 0.00 -> 28.7 mm, vias 0 -> 2
- net Net-(C74-Pad1): track 25.7 -> 0.00 mm
- net -8: track 228.1 -> 253.2 mm, vias 12 -> 15
- net /Microcontroller/+5VMON: track 0.00 -> 24.0 mm, vias 0 -> 2
- net +5: track 483.8 -> 507.5 mm, vias 39 -> 36
- net Net-(C68-Pad1): track 20.4 -> 0.00 mm
- net +8: track 235.6 -> 256.0 mm, vias 14 -> 15
- net /Microcontroller/-5VMON: track 0.00 -> 19.4 mm, vias 0 -> 2
- net -5: track 286.4 -> 270.6 mm, vias 28 -> 26
- net /Power/VRHS: track 32.6 -> 43.8 mm
- net /Channel1/ATT2: track 40.7 -> 33.5 mm
- net +3.3A: track 27.1 -> 33.8 mm, vias 0 -> 2
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- added copper zone on F.Cu, net +8
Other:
- board text added: "MCU SWD"
- board text added: "THIS SPACE ACCIDENTALLY LEFT BLANK"
- board text added: "THIS UP"
- board text added: "WAY"

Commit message: Route #IRQ and #PERST
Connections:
- J9 pad A11: /#PERST -> /Microcontroller/#PERST
- U10 pad 16: Net-(U10-Pad16) -> /Microcontroller/#IRQ
- U10 pad 17: Net-(U10-Pad17) -> /Microcontroller/#PERST
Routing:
- net /Microcontroller/#PERST: track 0.00 -> 110.4 mm, vias 0 -> 1
- net /Microcontroller/#IRQ: track 0.00 -> 107.7 mm, vias 0 -> 2
- net GND: track 1256.5 -> 1254.7 mm, vias 422 -> 421
- net /Microcontroller/SCL: track 105.0 -> 103.4 mm
- net /Channel1/ATT2: track 33.5 -> 35.1 mm
- net /Microcontroller/#SS: track 105.7 -> 104.5 mm
- net /Microcontroller/SDA: track 106.7 -> 105.8 mm
- net /Microcontroller/SCK: track 102.6 -> 101.6 mm
- net /Microcontroller/MOSI: track 104.4 -> 103.4 mm
- net /Microcontroller/CH1_GAIN2: track 46.9 -> 47.8 mm
- net /Microcontroller/MISO: track 104.9 -> 104.2 mm

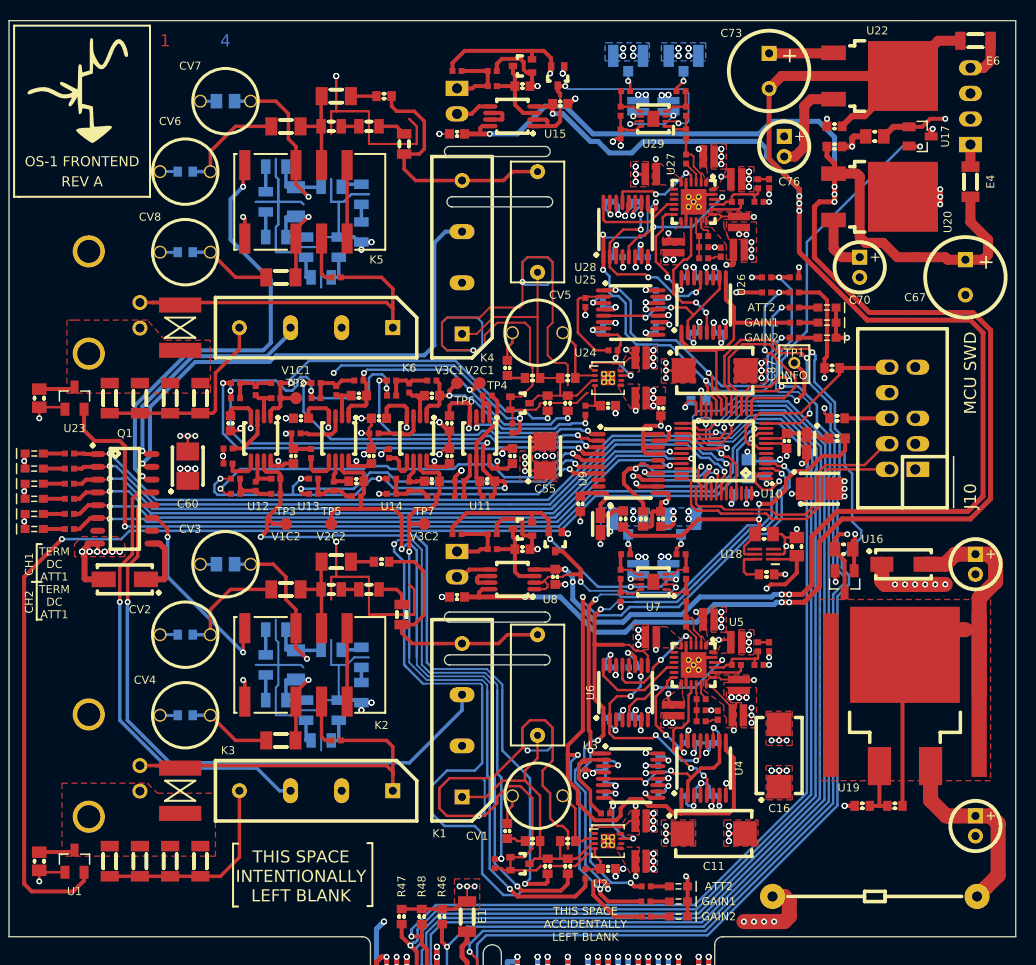
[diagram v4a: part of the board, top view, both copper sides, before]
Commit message: Reannotate schematic/PCB
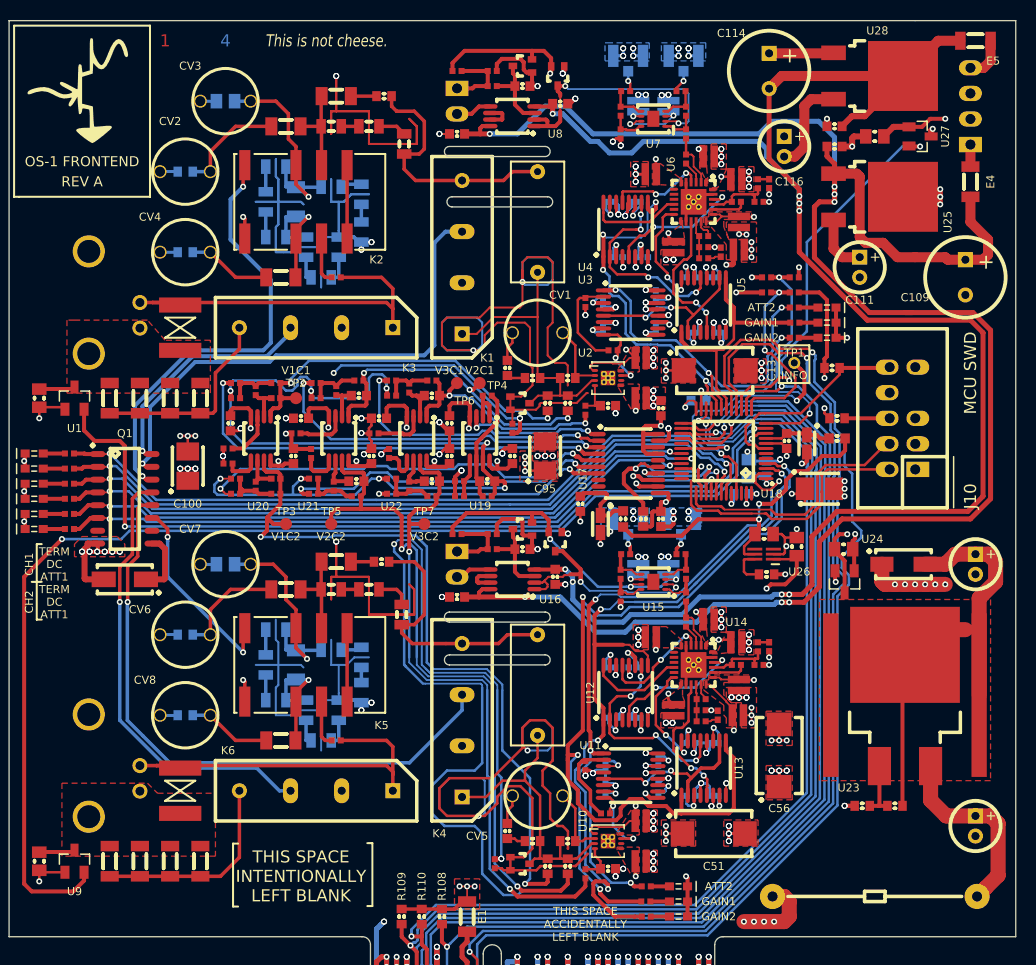
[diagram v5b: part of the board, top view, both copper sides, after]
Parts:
- removed the C61 at (105.8, 58.0)
- added C101: 100n, IPC7351-Nominal:CAPC1608X55, F.Cu at (105.8, 58.0)
- renumbered C77 to C1, C115 to C10, C60 to C100, C62 to C102, C63 to C103, C64 to C104, C65 to C105, C66 to C106, C118 to C107, C119 to C108, C67 to C109, C117 to C11, C68 to C110, C70 to C111, C71 to C112, C72 to C113, C73 to C114, C74 to C115, C76 to C116, C86 to C12, C87 to C13, C88 to C14, C89 to C15, C90 to C16, C91 to C17, C93 to C19, C78 to C2, C94 to C20, C95 to C21, C96 to C22, C97 to C23, C98 to C24, C99 to C25, C100 to C26, C101 to C27, C102 to C28, C103 to C29, C79 to C3, C104 to C30, C105 to C31, C106 to C32, C107 to C33, C108 to C34, C109 to C35, C110 to C36, C111 to C37, C112 to C38, C1 to C39, C80 to C4, C2 to C40, C3 to C41, C4 to C42, C5 to C43, C6 to C44, C7 to C45, C8 to C46, C9 to C47, C114 to C48, C116 to C49, C81 to C5, C10 to C50, C11 to C51, C12 to C52, C13 to C53, C14 to C54, C15 to C55, C16 to C56, C17 to C57, C18 to C58, C19 to C59, C82 to C6, C20 to C60, C21 to C61, C22 to C62, C23 to C63, C24 to C64, C25 to C65, C26 to C66, C27 to C67, C28 to C68, C29 to C69, C83 to C7, C30 to C70, C31 to C71, C32 to C72, C33 to C73, C34 to C74, C35 to C75, C36 to C76, C43 to C77, C44 to C78, C37 to C79, C84 to C8, C38 to C80, C39 to C81, C40 to C82, C41 to C83, C42 to C84, C113 to C85, C45 to C86, C47 to C87, C48 to C88, C49 to C89, C85 to C9, C50 to C90, C51 to C91, C52 to C92, C53 to C93, C54 to C94, C55 to C95, C56 to C96, C57 to C97, C58 to C98, C59 to C99, CV5 to CV1, CV6 to CV2, CV7 to CV3, CV8 to CV4, CV1 to CV5, CV2 to CV6, CV3 to CV7, CV4 to CV8, D5 to D1, D6 to D2, D7 to D3, D1 to D4, D2 to D5, D3 to D6, D4 to D7, E6 to E5, GDT2 to GDT1, GDT1 to GDT2, K4 to K1, K5 to K2, K6 to K3, K1 to K4, K2 to K5, K3 to K6, R86 to R1, R95 to R10, R44 to R100, R134 to R101, R135 to R102, R136 to R103, R137 to R104, R138 to R105, R139 to R106, R45 to R107, R46 to R108, R47 to R109, R96 to R11, R48 to R110, R49 to R111, R50 to R112, R51 to R113, R52 to R114, R53 to R115, R54 to R116, R55 to R117, R56 to R118, R57 to R119, R97 to R12, R58 to R120, R59 to R121, R60 to R122, R61 to R123, R62 to R124, R63 to R125, R64 to R126, R65 to R127, R66 to R128, R67 to R129, R98 to R13, R68 to R130, R69 to R131, R70 to R132, R71 to R133, R72 to R134, R73 to R135, R74 to R136, R75 to R137, R76 to R138, R77 to R139, R99 to R14, R78 to R140, R79 to R141, R80 to R142, R81 to R143, R82 to R144, R83 to R145, R84 to R146, R85 to R147, R100 to R15, R101 to R16, R102 to R17, R103 to R18, R104 to R19, R87 to R2, R105 to R20, R106 to R21, R107 to R22, R108 to R23, R109 to R24, R110 to R25, R111 to R26, R112 to R27, R113 to R28, R114 to R29, R88 to R3, R115 to R30, R116 to R31, R117 to R32, R118 to R33, R119 to R34, R120 to R35, R121 to R36, R141 to R37, R143 to R38, R122 to R39, R89 to R4, R123 to R40, R124 to R41, R125 to R42, R126 to R43, R127 to R44, R1 to R45, R2 to R46, R3 to R47, R4 to R48, R5 to R49, R90 to R5, R6 to R50, R7 to R51, R8 to R52, R9 to R53, R10 to R54, R11 to R55, R12 to R56, R13 to R57, R14 to R58, R15 to R59, R91 to R6, R16 to R60, R17 to R61, R18 to R62, R19 to R63, R20 to R64, R21 to R65, R22 to R66, R23 to R67, R24 to R68, R25 to R69, R92 to R7, R26 to R70, R27 to R71, R28 to R72, R29 to R73, R30 to R74, R31 to R75, R32 to R76, R33 to R77, R34 to R78, R35 to R79, R93 to R8, R36 to R80, R140 to R81, R142 to R82, R37 to R83, R38 to R84, R39 to R85, R40 to R86, R41 to R87, R42 to R88, R43 to R89, R94 to R9, R144 to R90, R145 to R91, R146 to R92, R147 to R93, R128 to R94, R129 to R95, R130 to R96, R131 to R97, R132 to R98, R133 to R99, U23 to U1, U2 to U10, U3 to U11, U6 to U12, U4 to U13, U5 to U14, U7 to U15, U8 to U16, U9 to U17, U10 to U18, U11 to U19, U24 to U2, U12 to U20, U13 to U21, U14 to U22, U19 to U23, U16 to U24, U20 to U25, U18 to U26, U17 to U27, U22 to U28, U25 to U3, U28 to U4, U26 to U5, U27 to U6, U29 to U7, U15 to U8, U1 to U9
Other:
- board text added: "This is not cheese."
